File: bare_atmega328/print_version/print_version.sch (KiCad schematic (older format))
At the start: 17 parts, among them J1 22-23-2021, J2 22-23-2021, J3 640456-3, J4 22-23-2021, J5 Conn_01x14_Male, J6 Conn_01x14_Male, J7 640456-3, SW1 SW_Push, U1 ATMEGA328-PU, Y1 Crystal

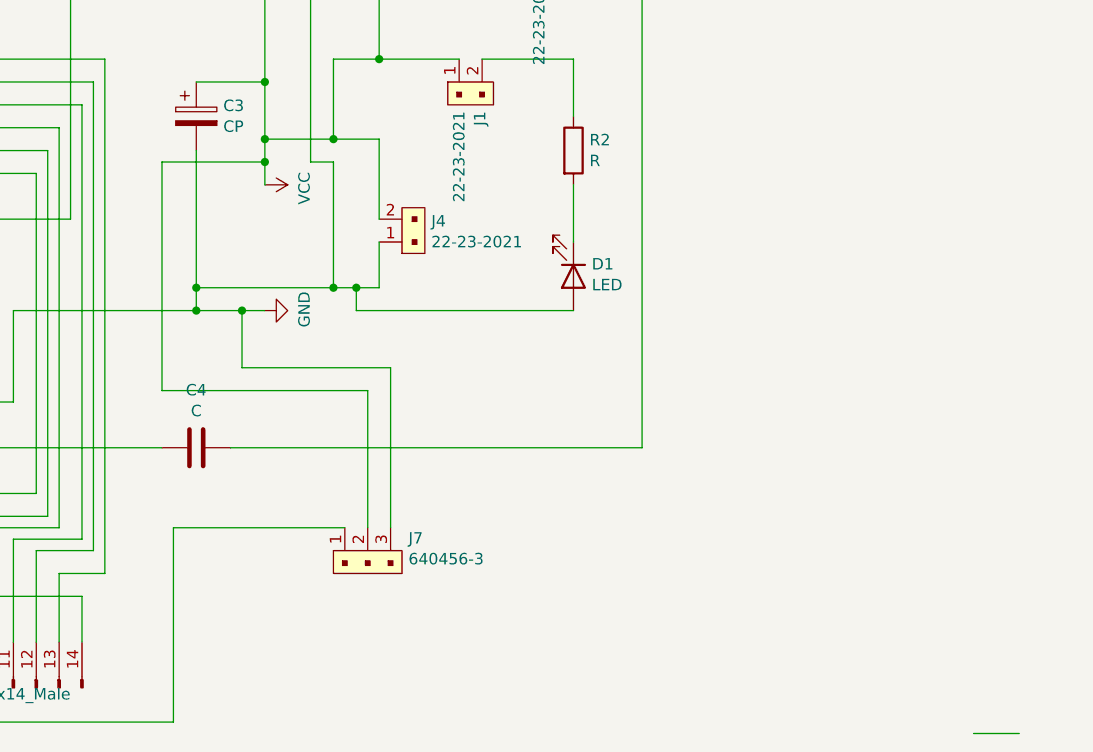
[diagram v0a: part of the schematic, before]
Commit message: Version with 555 dip
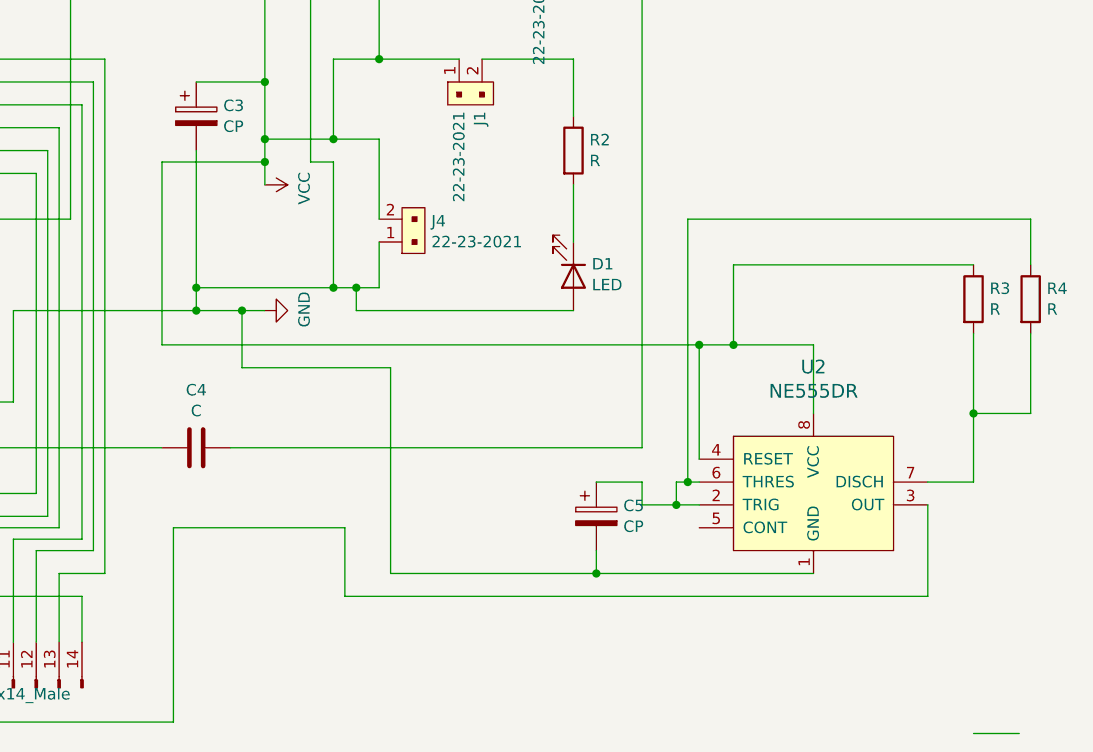
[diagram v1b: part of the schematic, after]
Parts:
- removed J7: 640456-3, Connector_PinHeader_2.54mm:PinHeader_1x03_P2.54mm_Vertical, symbol dk_Rectangular-Connectors-Headers-Male-Pins:640456-3
- added C5: CP, Capacitor_THT:CP_Radial_D5.0mm_P2.00mm, symbol Device:CP
- added R3, R4: R, Resistor_THT:R_Axial_DIN0204_L3.6mm_D1.6mm_P7.62mm_Horizontal, symbol Device:R
- added U2: NE555DR, Package_DIP:DIP-8_W7.62mm, symbol dk_Clock-Timing-Programmable-Timers-and-Oscillators:NE555DR
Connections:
- net GND: now also C5.2, U2.1 (GND)
- net VCC: now also R3.1, U2.4 (RESET), U2.8 (VCC)
- net at J6.4 (Pin_4), U1.4 (PD2): now also U2.3 (OUT)
- new net: C5.1, R4.1, U2.2 (TRIG), U2.6 (THRES)
- new net: R3.2, R4.2, U2.7 (DISCH)
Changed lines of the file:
@@
 	6600 4600 7050 4600
-Wire Wire Line
-	6600 5600 6600 4600
-Wire Wire Line
-	6600 5600 7500 5600
-Wire Wire Line
-	7500 5600 7500 6200
-Wire Wire Line
-	7600 5500 7600 6200
 Wire Wire Line
 	6950 5500 7600 5500
@@
 	6950 5500 6950 5250
 $Comp
-L dk_Rectangular-Connectors-Headers-Male-Pins:640456-3 J7
-U 1 1 5F766E81
-P 7400 6300
-F 0 "J7" H 7678 6354 50  0000 L CNN
-F 1 "640456-3" H 7678 6263 50  0000 L CNN
-F 2 "Connector_PinHeader_2.54mm:PinHeader_1x03_P2.54mm_Vertical" H 7600 6500 60  0001 L CNN
-F 3 "https://www.te.com/commerce/DocumentDelivery/DDEController?Action=srchrtrv&DocNm=640456&DocType=Customer+Drawing&DocLang=English" H 7600 6600 60  0001 L CNN
-F 4 "A19470-ND" H 7600 6700 60  0001 L CNN "Digi-Key_PN"
-F 5 "640456-3" H 7600 6800 60  0001 L CNN "MPN"
-F 6 "Connectors, Interconnects" H 7600 6900 60  0001 L CNN "Category"
-F 7 "Rectangular Connectors - Headers, Male Pins" H 7600 7000 60  0001 L CNN "Family"
-F 8 "https://www.te.com/commerce/DocumentDelivery/DDEController?Action=srchrtrv&DocNm=640456&DocType=Customer+Drawing&DocLang=English" H 7600 7100 60  0001 L CNN "DK_Datasheet_Link"
-F 9 "/product-detail/en/te-connectivity-amp-connectors/640456-3/A19470-ND/259010" H 7600 7200 60  0001 L CNN "DK_Detail_Page"
-F 10 "CONN HEADER VERT 3POS 2.54MM" H 7600 7300 60  0001 L CNN "Description"
-F 11 "TE Connectivity AMP Connectors" H 7600 7400 60  0001 L CNN "Manufacturer"
-F 12 "Active" H 7600 7500 60  0001 L CNN "Status"
-	1    7400 6300
+L dk_Clock-Timing-Programmable-Timers-and-Oscillators:NE555DR U2
+U 1 1 5F6E4887
+P 9450 5800
+F 0 "U2" H 9450 6103 60  0000 C CNN
+F 1 "NE555DR" H 9450 5997 60  0000 C CNN
+F 2 "Package_DIP:DIP-8_W7.62mm" H 9650 6000 60  0001 L CNN
+F 3 "http://www.ti.com/general/docs/suppproductinfo.tsp?distId=10&gotoUrl=http%3A%2F%2Fwww.ti.com%2Flit%2Fgpn%2Fne555" H 9650 6100 60  0001 L CNN
+F 4 "296-6501-1-ND" H 9650 6200 60  0001 L CNN "Digi-Key_PN"
+F 5 "NE555DR" H 9650 6300 60  0001 L CNN "MPN"
+F 6 "Integrated Circuits (ICs)" H 9650 6400 60  0001 L CNN "Category"
+F 7 "Clock/Timing - Programmable Timers and Oscillators" H 9650 6500 60  0001 L CNN "Family"
+F 8 "http://www.ti.com/general/docs/suppproductinfo.tsp?distId=10&gotoUrl=http%3A%2F%2Fwww.ti.com%2Flit%2Fgpn%2Fne555" H 9650 6600 60  0001 L CNN "DK_Datasheet_Link"
+F 9 "/product-detail/en/texas-instruments/NE555DR/296-6501-1-ND/372490" H 9650 6700 60  0001 L CNN "DK_Detail_Page"
+F 10 "IC OSC SGL TIMER 100KHZ 8-SOIC" H 9650 6800 60  0001 L CNN "Description"
+F 11 "Texas Instruments" H 9650 6900 60  0001 L CNN "Manufacturer"
+F 12 "Active" H 9650 7000 60  0001 L CNN "Status"
+	1    9450 5800
 	1    0    0    -1
 $EndComp
+Wire Wire Line
+	9450 6400 8500 6400
+Wire Wire Line
+	7600 5500 7600 6400
+Wire Wire Line
+	9450 5700 9450 5400
+Wire Wire Line
+	9450 5400 9100 5400
+Wire Wire Line
+	6600 4600 6600 5400
+Wire Wire Line
+	9950 6100 9950 6500
+Wire Wire Line
+	9950 6500 7400 6500
+Wire Wire Line
+	7400 6500 7400 6200
+$Comp
+L Device:CP C5
+U 1 1 5F7630F7
+P 8500 6150
+F 0 "C5" H 8618 6196 50  0000 L CNN
+F 1 "CP" H 8618 6105 50  0000 L CNN
+F 2 "Capacitor_THT:CP_Radial_D5.0mm_P2.00mm" H 8538 6000 50  0001 C CNN
+F 3 "~" H 8500 6150 50  0001 C CNN
+	1    8500 6150
+	1    0    0    -1
+$EndComp
+Wire Wire Line
+	8950 6100 8850 6100
+Wire Wire Line
+	8700 6100 8700 6000
+Wire Wire Line
+	8700 6000 8500 6000
+Wire Wire Line
+	8500 6300 8500 6400
+Connection ~ 8500 6400
+Wire Wire Line
+	8500 6400 7600 6400
+Wire Wire Line
+	8950 6000 8900 6000
+Wire Wire Line
+	8850 6000 8850 6100
+Connection ~ 8850 6100
+Wire Wire Line
+	8850 6100 8700 6100
+$Comp
+L Device:R R3
+U 1 1 5F78B7B5
+P 10150 5200
+F 0 "R3" H 10220 5246 50  0000 L CNN
+F 1 "R" H 10220 5155 50  0000 L CNN
+F 2 "Resistor_THT:R_Axial_DIN0204_L3.6mm_D1.6mm_P7.62mm_Horizontal" V 10080 5200 50  0001 C CNN
+F 3 "~" H 10150 5200 50  0001 C CNN
+	1    10150 5200
+	1    0    0    -1
+$EndComp
+$Comp
+L Device:R R4
+U 1 1 5F78C478
+P 10400 5200
+F 0 "R4" H 10470 5246 50  0000 L CNN
+F 1 "R" H 10470 5155 50  0000 L CNN
+F 2 "Resistor_THT:R_Axial_DIN0204_L3.6mm_D1.6mm_P7.62mm_Horizontal" V 10330 5200 50  0001 C CNN
+F 3 "~" H 10400 5200 50  0001 C CNN
+	1    10400 5200
+	1    0    0    -1
+$EndComp
+Wire Wire Line
+	10150 5050 9100 5050
+Wire Wire Line
+	9100 5050 9100 5400
+Connection ~ 9100 5400
+Wire Wire Line
+	9100 5400 8950 5400
+Wire Wire Line
+	10150 5350 10150 5700
+Wire Wire Line
+	10150 6000 9950 6000
+Wire Wire Line
+	10400 5350 10400 5700
+Wire Wire Line
+	10400 5700 10150 5700
+Connection ~ 10150 5700
+Wire Wire Line
+	10150 5700 10150 6000
+Wire Wire Line
+	10400 5050 10400 4850
+Wire Wire Line
+	10400 4850 8900 4850
+Wire Wire Line
+	8900 4850 8900 6000
+Connection ~ 8900 6000
+Wire Wire Line
+	8900 6000 8850 6000
+Wire Wire Line
+	8950 5900 8950 5400
+Connection ~ 8950 5400
+Wire Wire Line
+	8950 5400 6600 5400
 $EndSCHEMATC

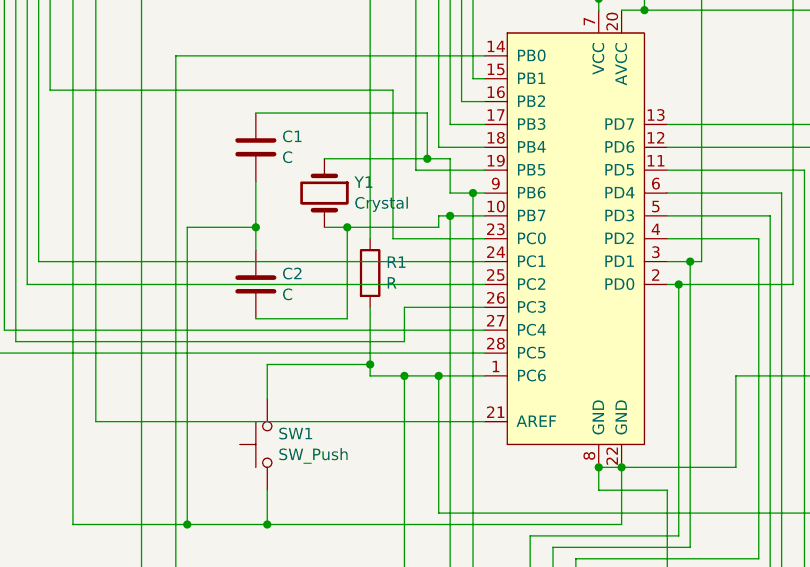
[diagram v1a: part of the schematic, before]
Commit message: Version v1.2 atmega328 + 555 timer
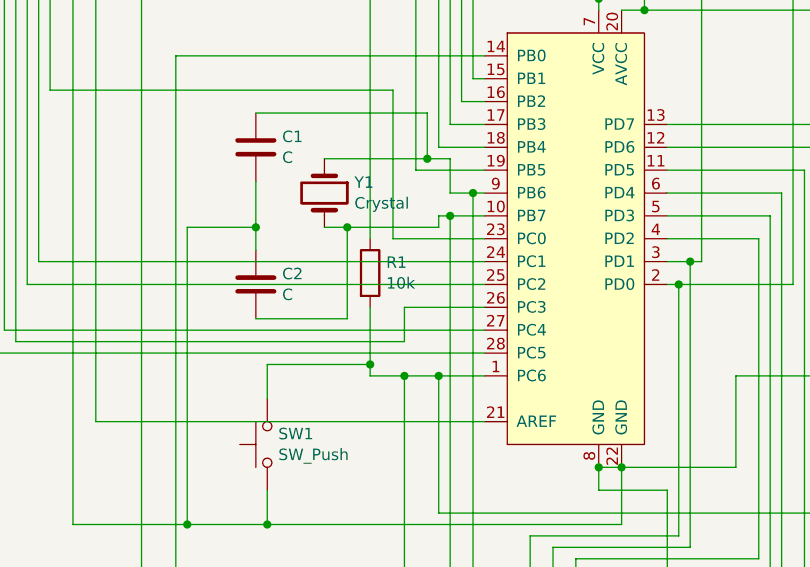
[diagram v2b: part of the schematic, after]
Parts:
- R1: value R -> 10k
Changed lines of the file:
@@
 P 4350 4800
 F 0 "R1" H 4420 4846 50  0000 L CNN
-F 1 "R" H 4420 4755 50  0000 L CNN
+F 1 "10k" H 4420 4755 50  0000 L CNN
 F 2 "Resistor_THT:R_Axial_DIN0204_L3.6mm_D1.6mm_P7.62mm_Horizontal" V 4280 4800 50  0001 C CNN
 F 3 "~" H 4350 4800 50  0001 C CNN
